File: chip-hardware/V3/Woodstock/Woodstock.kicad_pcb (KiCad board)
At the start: 2 copper layers, 16.5 x 19.1 mm, 11 parts, among them J1 501461-0491, U1 MCP9808_MSOP, U2 LIS3DH

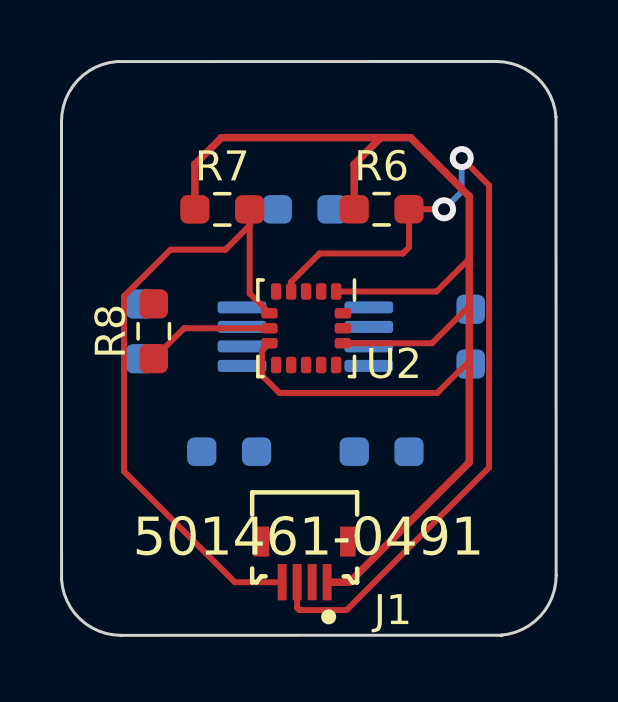
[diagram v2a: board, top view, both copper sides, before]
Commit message: Added traces to the back.
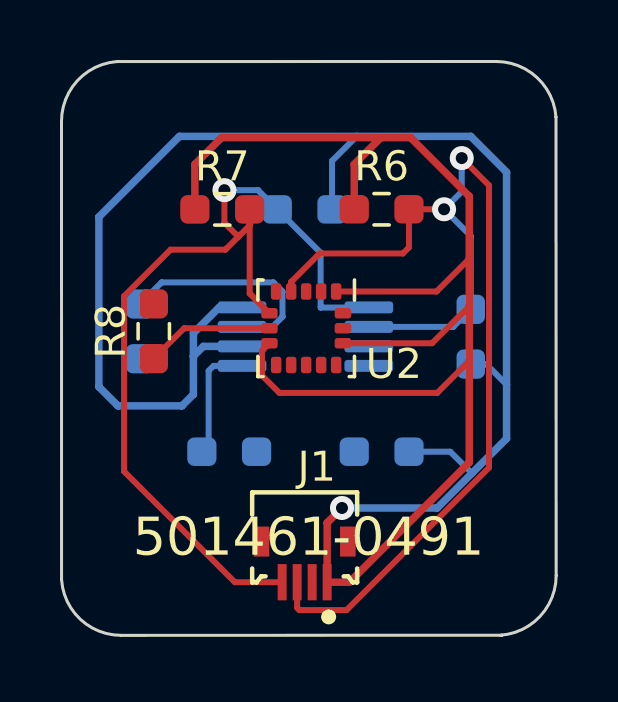
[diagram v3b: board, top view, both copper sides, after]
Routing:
- net +3V3: track 48.2 -> 103.1 mm, vias 0 -> 1
- net /SDA: track 22.1 -> 31.3 mm, vias 0 -> 1
- net Net-(R2-Pad1): track 0.00 -> 7.50 mm
- net /SCL: track 29.1 -> 36.4 mm
- net Net-(R5-Pad1): track 0.00 -> 3.97 mm
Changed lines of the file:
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@@
     (property "vault revision" "5F166C2B-E9D9-4135-9ADB-F1D93D2D935E")
     (attr through_hole)
-    (fp_text reference "J1" (at -3.5814 -1.6105) (layer "F.SilkS")
+    (fp_text reference "J1" (at -1.04084 3.16856) (layer "F.SilkS")
       (effects (font (size 1 1) (thickness 0.15)) (justify right))
     )
@@
       (effects (font (size 1 1) (thickness 0.15)))
     )
-    (fp_text value "LIS3DH" (at 2.6924 0.7366 180) (layer "F.Fab")
+    (fp_text value "LIS3DH" (at 2.6924 0.00056 180) (layer "F.Fab")
       (effects (font (size 1 1) (thickness 0.15)))
     )
@@
     (property "Sheetname" "")
     (attr smd)
-    (fp_text reference "U1" (at 4.3434 -2.6162) (layer "B.SilkS")
+    (fp_text reference "U1" (at -0.02484 -2.45994) (layer "B.SilkS")
       (effects (font (size 1 1) (thickness 0.15)) (justify mirror))
     )
@@
     (property "Sheetname" "")
     (attr smd)
-    (fp_text reference "R3" (at 0 1.43) (layer "B.SilkS")
-      (effects (font (size 1 1) (thickness 0.15)) (justify mirror))
-    )
-    (fp_text value "10k" (at 0 -1.43) (layer "B.Fab")
+    (fp_text reference "R3" (at 0.02596 1.40086) (layer "B.SilkS")
+      (effects (font (size 1 1) (thickness 0.15)) (justify mirror))
+    )
+    (fp_text value "10k" (at -2.97124 0.02926) (layer "B.Fab")
       (effects (font (size 1 1) (thickness 0.15)) (justify mirror))
     )
@@
     (property "Sheetname" "")
     (attr smd)
-    (fp_text reference "R5" (at 0 1.43) (layer "B.SilkS")
-      (effects (font (size 1 1) (thickness 0.15)) (justify mirror))
-    )
-    (fp_text value "10k" (at 0 -1.43) (layer "B.Fab")
+    (fp_text reference "R5" (at 0 -1.42626) (layer "B.SilkS")
+      (effects (font (size 1 1) (thickness 0.15)) (justify mirror))
+    )
+    (fp_text value "10k" (at 0.02484 1.49474) (layer "B.Fab")
       (effects (font (size 1 1) (thickness 0.15)) (justify mirror))
     )
@@
   (segment (start 148.676862 104.658662) (end 144.9832 100.965) (width 0.2) (layer "F.Cu") (net 3))
   (segment (start 144.9832 100.965) (end 144.9832 95.12506) (width 0.2) (layer "F.Cu") (net 3))
+  (segment (start 148.329225 92.677825) (end 148.7932 93.1418) (width 0.2) (layer "F.Cu") (net 3))
+  (segment (start 148.3614 93.5736) (end 148.7932 93.1418) (width 0.2) (layer "F.Cu") (net 3))
   (segment (start 149.82936 95.69366) (end 149.1704 95.0347) (width 0.2) (layer "F.Cu") (net 3))
   (segment (start 150.253559 104.658662) (end 148.676862 104.658662) (width 0.2) (layer "F.Cu") (net 3))
-  (segment (start 148.3614 93.5736) (end 149.1704 92.7646) (width 0.2) (layer "F.Cu") (net 3))
   (segment (start 146.53466 93.5736) (end 148.3614 93.5736) (width 0.2) (layer "F.Cu") (net 3))
   (segment (start 149.1704 92.7646) (end 149.1704 92.23126) (width 0.2) (layer "F.Cu") (net 3))
+  (segment (start 148.329225 91.591179) (end 148.329225 92.677825) (width 0.2) (layer "F.Cu") (net 3))
+  (segment (start 148.7932 93.1418) (end 149.1704 92.7646) (width 0.2) (layer "F.Cu") (net 3))
+  (via (at 148.329225 91.591179) (size 0.8) (drill 0.4) (layers "F.Cu" "B.Cu") (net 3))
+  (segment (start 150.09106 92.23126) (end 149.450979 91.591179) (width 0.2) (layer "B.Cu") (net 3))
+  (segment (start 153.13552 95.504) (end 153.14146 95.49806) (width 0.2) (layer "B.Cu") (net 3))
+  (segment (start 150.09106 92.23126) (end 151.5364 93.6766) (width 0.2) (layer "B.Cu") (net 3))
+  (segment (start 149.450979 91.591179) (end 148.329225 91.591179) (width 0.2) (layer "B.Cu") (net 3))
+  (segment (start 151.5364 93.6766) (end 151.5364 95.504) (width 0.2) (layer "B.Cu") (net 3))
+  (segment (start 151.5364 95.504) (end 153.13552 95.504) (width 0.2) (layer "B.Cu") (net 3))
   (segment (start 151.500092 93.7006) (end 154.2796 93.7006) (width 0.2) (layer "F.Cu") (net 4))
   (segment (start 154.2796 93.7006) (end 154.4809 93.4993) (width 0.2) (layer "F.Cu") (net 4))
@@
   (via (at 156.239699 90.521301) (size 0.8) (drill 0.4) (layers "F.Cu" "B.Cu") (net 4))
   (via (at 155.6512 92.2274) (size 0.8) (drill 0.4) (layers "F.Cu" "B.Cu") (net 4))
+  (segment (start 155.95516 96.14806) (end 153.14146 96.14806) (width 0.2) (layer "B.Cu") (net 4))
   (segment (start 156.239699 91.638901) (end 155.6512 92.2274) (width 0.2) (layer "B.Cu") (net 4))
+  (segment (start 156.54076 95.56246) (end 155.95516 96.14806) (width 0.2) (layer "B.Cu") (net 4))
   (segment (start 156.239699 90.521301) (end 156.239699 91.638901) (width 0.2) (layer "B.Cu") (net 4))
+  (segment (start 156.54076 93.11696) (end 155.6512 92.2274) (width 0.2) (layer "B.Cu") (net 4))
+  (segment (start 156.54076 95.56246) (end 156.54076 93.11696) (width 0.2) (layer "B.Cu") (net 4))
   (segment (start 156.4894 95.4532) (end 156.4894 93.8784) (width 0.25) (layer "F.Cu") (net 6))
   (segment (start 149.57984 97.766468) (end 150.162172 98.3488) (width 0.2) (layer "F.Cu") (net 6))
@@
   (segment (start 152.497577 104.658662) (end 156.4894 100.666839) (width 0.25) (layer "F.Cu") (net 6))
   (segment (start 147.3454 90.7288) (end 147.3454 92.23126) (width 0.25) (layer "F.Cu") (net 6))
+  (segment (start 151.753559 102.678241) (end 152.2476 102.1842) (width 0.25) (layer "F.Cu") (net 6))
   (segment (start 152.05436 94.96866) (end 155.39914 94.96866) (width 0.2) (layer "F.Cu") (net 6))
   (segment (start 153.543 89.8398) (end 148.2344 89.8398) (width 0.25) (layer "F.Cu") (net 6))
@@
   (segment (start 156.4894 93.8784) (end 156.4894 91.7956) (width 0.25) (layer "F.Cu") (net 6))
   (segment (start 155.39914 94.96866) (end 156.4894 93.8784) (width 0.2) (layer "F.Cu") (net 6))
+  (segment (start 151.753559 104.658662) (end 151.753559 102.678241) (width 0.25) (layer "F.Cu") (net 6))
   (segment (start 151.753559 104.658662) (end 152.497577 104.658662) (width 0.25) (layer "F.Cu") (net 6))
   (segment (start 156.4894 97.282) (end 156.4894 95.4532) (width 0.25) (layer "F.Cu") (net 6))
@@
   (segment (start 149.57984 96.94318) (end 149.57984 97.766468) (width 0.2) (layer "F.Cu") (net 6))
   (segment (start 156.4894 100.666839) (end 156.4894 97.282) (width 0.25) (layer "F.Cu") (net 6))
+  (via (at 152.2476 102.1842) (size 0.8) (drill 0.4) (layers "F.Cu" "B.Cu") (net 6))
+  (segment (start 157.734 99.8728) (end 157.734 98.0694) (width 0.25) (layer "B.Cu") (net 6))
+  (segment (start 156.539802 89.79679) (end 152.73799 89.79679) (width 0.25) (layer "B.Cu") (net 6))
+  (segment (start 157.05206 97.38746) (end 157.734 98.0694) (width 0.2) (layer "B.Cu") (net 6))
+  (segment (start 147.2946 96.357059) (end 148.153599 95.49806) (width 0.25) (layer "B.Cu") (net 6))
+  (segment (start 151.91606 90.61872) (end 152.73799 89.79679) (width 0.2) (layer "B.Cu") (net 6))
+  (segment (start 144.78 98.7806) (end 146.9136 98.7806) (width 0.25) (layer "B.Cu") (net 6))
+  (segment (start 157.734 98.0694) (end 157.734 90.990988) (width 0.25) (layer "B.Cu") (net 6))
+  (segment (start 147.2946 98.3996) (end 147.2946 97.1296) (width 0.25) (layer "B.Cu") (net 6))
+  (segment (start 147.2946 97.1296) (end 147.2946 96.357059) (width 0.25) (layer "B.Cu") (net 6))
+  (segment (start 144.145 92.4814) (end 144.145 98.1456) (width 0.25) (layer "B.Cu") (net 6))
+  (segment (start 156.5783 101.0285) (end 157.734 99.8728) (width 0.25) (layer "B.Cu") (net 6))
+  (segment (start 148.153599 95.49806) (end 148.91646 95.49806) (width 0.25) (layer "B.Cu") (net 6))
+  (segment (start 144.145 98.1456) (end 144.78 98.7806) (width 0.25) (layer "B.Cu") (net 6))
+  (segment (start 152.2476 102.1842) (end 155.4226 102.1842) (width 0.25) (layer "B.Cu") (net 6))
+  (segment (start 155.4226 102.1842) (end 156.5783 101.0285) (width 0.25) (layer "B.Cu") (net 6))
+  (segment (start 156.54076 97.38746) (end 157.05206 97.38746) (width 0.2) (layer "B.Cu") (net 6))
+  (segment (start 147.62614 96.79806) (end 148.91646 96.79806) (width 0.25) (layer "B.Cu") (net 6))
+  (segment (start 146.82961 89.79679) (end 144.145 92.4814) (width 0.25) (layer "B.Cu") (net 6))
+  (segment (start 154.48146 100.30846) (end 155.85826 100.30846) (width 0.2) (layer "B.Cu") (net 6))
+  (segment (start 146.9136 98.7806) (end 147.2946 98.3996) (width 0.25) (layer "B.Cu") (net 6))
+  (segment (start 155.85826 100.30846) (end 156.5783 101.0285) (width 0.2) (layer "B.Cu") (net 6))
+  (segment (start 147.2946 97.1296) (end 147.62614 96.79806) (width 0.25) (layer "B.Cu") (net 6))
+  (segment (start 151.91606 92.23126) (end 151.91606 90.61872) (width 0.2) (layer "B.Cu") (net 6))
+  (segment (start 152.73799 89.79679) (end 146.82961 89.79679) (width 0.25) (layer "B.Cu") (net 6))
+  (segment (start 157.734 90.990988) (end 156.539802 89.79679) (width 0.25) (layer "B.Cu") (net 6))
+  (segment (start 149.92714 96.14806) (end 148.91646 96.14806) (width 0.2) (layer "B.Cu") (net 7))
+  (segment (start 149.9616 94.6658) (end 150.2664 94.9706) (width 0.2) (layer "B.Cu") (net 7))
+  (segment (start 145.51716 95.38466) (end 146.23602 94.6658) (width 0.2) (layer "B.Cu") (net 7))
+  (segment (start 150.2664 95.8088) (end 149.92714 96.14806) (width 0.2) (layer "B.Cu") (net 7))
+  (segment (start 146.23602 94.6658) (end 149.9616 94.6658) (width 0.2) (layer "B.Cu") (net 7))
+  (segment (start 150.2664 94.9706) (end 150.2664 95.8088) (width 0.2) (layer "B.Cu") (net 7))
+  (segment (start 147.8026 97.6122) (end 147.8026 100.08232) (width 0.2) (layer "B.Cu") (net 8))
+  (segment (start 148.91646 97.44806) (end 147.96674 97.44806) (width 0.2) (layer "B.Cu") (net 8))
+  (segment (start 147.96674 97.44806) (end 147.8026 97.6122) (width 0.2) (layer "B.Cu") (net 8))
+  (segment (start 147.8026 100.08232) (end 147.57646 100.30846) (width 0.2) (layer "B.Cu") (net 8))
   (segment (start 145.97436 97.20586) (end 146.98656 96.19366) (width 0.2) (layer "F.Cu") (net 9))
   (segment (start 146.98656 96.19366) (end 149.82936 96.19366) (width 0.2) (layer "F.Cu") (net 9))
